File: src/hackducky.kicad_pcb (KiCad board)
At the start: 2 copper layers, 21 x 47 mm, 51 parts, among them J1 USB_A, J2 Conn_02x02_Top_Bottom, J3 Micro_SD_Card, P2 USB_C_Plug, SW3 BOOT_SEL, SW4 BOOT_SEL, U1 W25Q16JVSS, U2 AP2112K-3.3, U3 USBLC6-2P6, U4 RP2040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

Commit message: new sm fic
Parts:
- moved G*** 1.70 mm to (82.7, 95.0) (x2)
- moved G*** 0.26 mm to (82.1, 93.0)
- moved G*** 0.25 mm to (82.1, 93.0)
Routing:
- net +3V3: track 154.5 -> 138.2 mm, vias 23 -> 20
- net GPIO0: track 19.9 -> 14.4 mm, vias 3 -> 1
- net D-: track 47.8 -> 44.9 mm, vias 4 -> 2
- net D+: track 47.8 -> 44.9 mm, vias 4 -> 2
- net GND: track 189.5 -> 191.8 mm, vias 32 -> 29
- net GPIO11: track 6.53 -> 4.35 mm
- net SD_CLK: track 18.8 -> 19.6 mm
- net QSPI_SS: track 9.80 -> 10.5 mm, vias 3 -> 2
- net +5V: track 74.1 -> 74.4 mm, vias 6 -> 8
- added copper zone on B.Cu, net +3V3

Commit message: new
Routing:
- net GND: vias 29 -> 31
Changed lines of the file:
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@@
+	)
+	(via
+		(at 90 80.75)
+		(size 0.5)
+		(drill 0.3)
+		(layers "F.Cu" "B.Cu")
+		(net 1)
 	)
 	(via
@@
 		(drill 0.3)
 		(layers "F.Cu" "B.Cu")
+		(net 1)
+	)
+	(via
+		(at 90 80.75)
+		(size 0.5)
+		(drill 0.3)
+		(layers "F.Cu" "B.Cu")

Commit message: new
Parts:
- removed the G*** at (82.1, 93.0) (x2)
- removed the G*** at (82.7, 95.0) (x2)
- moved C12 1.81 mm to (82.8, 87.1), turned to 0 degrees
- moved R9 1.42 mm to (88.5, 85.8)
- moved C13 1.21 mm to (86.5, 85.5), turned to 180 degrees
- moved Y1 1.10 mm to (83.4, 84.9)
- moved D4 0.43 mm to (82.0, 81.8)
- moved D1 0.40 mm to (99.0, 80.5)
- moved R22 0.11 mm to (92.5, 74.6)
- moved R7 0.11 mm to (91.4, 74.6)
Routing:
- net +3V3: track 138.2 -> 128.6 mm, vias 20 -> 18
- net +1V1: track 27.8 -> 20.8 mm
- net Net-(C12-Pad1): track 7.71 -> 1.36 mm
- net GND: track 191.8 -> 186.2 mm, vias 31 -> 20
- net SD_CLK: track 19.6 -> 21.1 mm
- net XOUT: track 3.36 -> 1.89 mm
- net SD_MOSI: track 21.0 -> 22.2 mm
- net GP25: track 6.62 -> 5.98 mm

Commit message: fixed silkscren
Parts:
- added G*** (x2): LOGO, LOGO, F.Cu at (83.3, 92.8)
- added G*** (x2): LOGO, LOGO, B.Cu at (83.5, 95.9)

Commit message: new
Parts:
- moved C8 7.19 mm to (91.0, 79.3)
- moved C16 1.26 mm to (84.4, 68.0)
- moved G*** 0.29 mm to (82.6, 65.5)
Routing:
- net Net-(C12-Pad1): track 1.36 -> 8.22 mm
- net +1V1: track 20.8 -> 17.7 mm, vias 2 -> 3
- net +3V3: track 128.6 -> 125.5 mm
- net GND: track 186.2 -> 187.9 mm
- net QSPI_SS: track 10.5 -> 9.81 mm

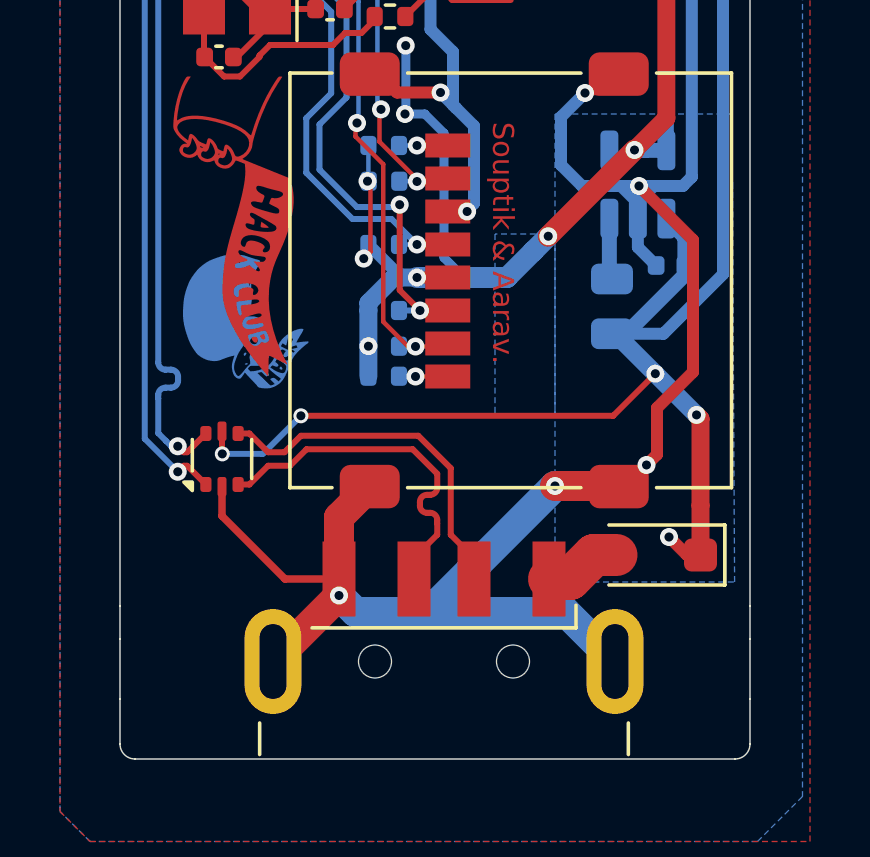
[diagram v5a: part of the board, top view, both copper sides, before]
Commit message: with bom corrected
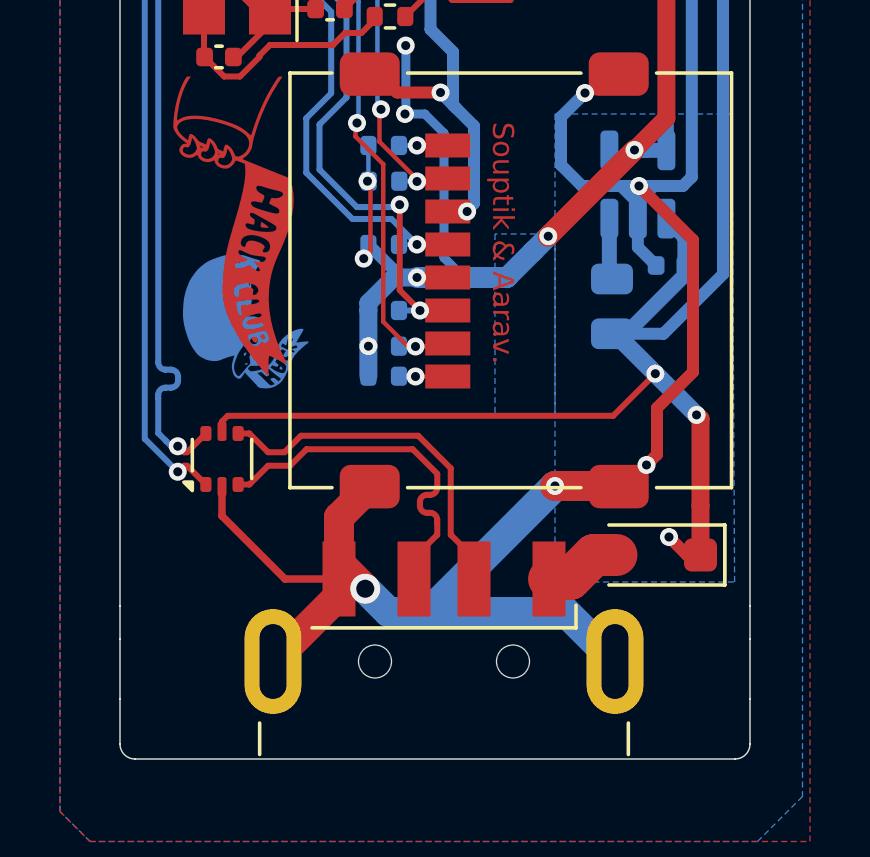
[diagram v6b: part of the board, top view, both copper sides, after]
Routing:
- net GND: track 187.9 -> 189.9 mm
- net +5V: track 74.4 -> 73.5 mm, vias 8 -> 6
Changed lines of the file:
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@@
 			(layer "F.Fab")
 		)
+		(fp_text user "${REFERENCE}"
+			(at 0 0 90)
+			(unlocked yes)
+			(layer "F.Fab")
+			(effects
+				(font
+					(size 1 1)
+					(thickness 0.15)
+				)
+			)
+		)
 		(pad "1" smd rect
 			(at -3.205 -2.1 90)
@@
 		)
 		(embedded_fonts no)
-		(model "${KICAD9_3DMODEL_DIR}/Connector_Card.3dshapes/microSD_HC_Hirose_DM3AT-SF-PEJM5.wrl"
+		(model "${KICAD9_3DMODEL_DIR}/Connector_Card.3dshapes/microSD_HC_Molex_47219-2001.wrl"
 			(offset
 				(xyz 0 0 0)
@@
 	)
 	(segment
+		(start 96.8 91.4)
+		(end 98.6 93.2)
+		(width 0.4)
+		(layer "F.Cu")
+		(net 1)
+	)
+	(segment
 		(start 96.105 101.4)
 		(end 96.125 101.42)
@@
 	)
 	(segment
-		(start 97.4 98.8)
-		(end 97.4 100.35)
-		(width 0.4)
-		(layer "F.Cu")
-		(net 1)
-	)
-	(segment
 		(start 83.52 79.25)
 		(end 83.35 79.25)
@@
 	)
 	(segment
+		(start 98.6 97.6)
+		(end 97.4 98.8)
+		(width 0.4)
+		(layer "F.Cu")
+		(net 1)
+	)
+	(segment
 		(start 94.11 73.69)
 		(end 94.2 73.69)
@@
 	)
 	(segment
-		(start 96.8 91.4)
-		(end 98.6 93.2)
-		(width 0.4)
-		(layer "F.Cu")
-		(net 1)
-	)
-	(segment
 		(start 94 101.4)
 		(end 96.105 101.4)
@@
 	)
 	(segment
+		(start 97.4 98.8)
+		(end 97.4 100.35)
+		(width 0.4)
+		(layer "F.Cu")
+		(net 1)
+	)
+	(segment
 		(start 90.16 72.5)
 		(end 90.16 70.325)
@@
 	)
 	(segment
-		(start 98.6 93.2)
-		(end 98.6 97.6)
-		(width 0.4)
-		(layer "F.Cu")
-		(net 1)
-	)
-	(segment
 		(start 88.98 68.3)
 		(end 88.98 67.75)
@@
 	)
 	(segment
+		(start 86.8 105.05)
+		(end 86.8 104.5)
+		(width 1)
+		(layer "F.Cu")
+		(net 1)
+	)
+	(segment
 		(start 84.5 86)
 		(end 84.5 85.75)
@@
 	)
 	(segment
+		(start 86.8 103.95)
+		(end 86.8 102.445)
+		(width 1)
+		(layer "F.Cu")
+		(net 1)
+	)
+	(segment
 		(start 85.286188 67.75)
 		(end 86.02 67.75)
@@
 	)
 	(segment
+		(start 87.675 104.825)
+		(end 86.8 103.95)
+		(width 1)
+		(layer "F.Cu")
+		(net 1)
+	)
+	(segment
 		(start 93.475 70.3)
 		(end 95.6 70.3)
@@
 	)
 	(segment
-		(start 86.8 104.5)
-		(end 86.8 105.05)
-		(width 1)
+		(start 98.6 93.2)
+		(end 98.6 97.6)
+		(width 0.4)
 		(layer "F.Cu")
 		(net 1)
@@
 	)
 	(segment
-		(start 83.28 87.1)
-		(end 83.4 87.1)
-		(width 0.2)
-		(layer "F.Cu")
-		(net 1)
-	)
-	(segment
-		(start 86.8 105.05)
-		(end 84.6 107.25)
+		(start 84.6 107.25)
+		(end 86.8 105.05)
 		(width 1)
 		(layer "F.Cu")
@@
 	)
 	(segment
-		(start 98.6 97.6)
-		(end 97.4 98.8)
-		(width 0.4)
+		(start 83.28 87.1)
+		(end 83.4 87.1)
+		(width 0.2)
 		(layer "F.Cu")
 		(net 1)
@@
 	)
 	(via
+		(at 87.675 104.825)
+		(size 1)
+		(drill 0.6)
+		(layers "F.Cu" "B.Cu")
+		(net 1)
+	)
+	(via
 		(at 83.1 79)
 		(size 0.6)
@@
 	)
 	(via
-		(at 86.8 105.05)
-		(size 0.6)
-		(drill 0.3)
-		(layers "F.Cu" "B.Cu")
-		(net 1)
-	)
-	(via
 		(at 96.8 91.4)
 		(size 0.6)
@@
 	)
 	(segment
+		(start 87.675 104.825)
+		(end 88.45 105.6)
+		(width 1)
+		(layer "B.Cu")
+		(net 1)
+	)
+	(segment
 		(start 87.229 65.121)
 		(end 87 65.35)
@@
 	)
 	(segment
-		(start 87.35 105.6)
-		(end 89.8 105.6)
-		(width 1)
-		(layer "B.Cu")
-		(net 1)
-	)
-	(segment
 		(start 94.2 90.7)
 		(end 94.9 91.4)
@@
 	)
 	(segment
+		(start 96.8 91.4)
+		(end 97.4 91.4)
+		(width 0.4)
+		(layer "B.Cu")
+		(net 1)
+	)
+	(segment
 		(start 98.55 79.5)
 		(end 98.56 79.51)
@@
 	)
 	(segment
-		(start 96.8 91.4)
-		(end 97.4 91.4)
-		(width 0.4)
-		(layer "B.Cu")
-		(net 1)
-	)
-	(segment
 		(start 98.56 91.1)
 		(end 98.26 91.4)
@@
 	)
 	(segment
+		(start 96.7625 91.4375)
+		(end 96.7625 92.4875)
+		(width 0.4)
+		(layer "B.Cu")
+		(net 1)
+	)
+	(segment
 		(start 90.16 70.99)
 		(end 90.4 70.75)
@@
 	)
 	(segment
-		(start 96.7625 92.4875)
-		(end 96.7625 91.4375)
-		(width 0.4)
-		(layer "B.Cu")
-		(net 1)
-	)
-	(segment
 		(start 92.729 64.64)
 		(end 92.729 65.079)
@@
 	)
 	(segment
+		(start 88.45 105.6)
+		(end 89.8 105.6)
+		(width 1)
+		(layer "B.Cu")
+		(net 1)
+	)
+	(segment
+		(start 96.8 91.4)
+		(end 96.7625 91.4375)
+		(width 0.4)
+		(layer "B.Cu")
+		(net 1)
+	)
+	(segment
 		(start 90.6 88.7)
 		(end 90.6 86.93)
@@
 	)
 	(segment
-		(start 96.7625 91.4375)
+		(start 96.2 91.4)
 		(end 96.8 91.4)
 		(width 0.4)
@@
 	)
 	(segment
-		(start 86.8 105.05)
-		(end 87.35 105.6)
-		(width 1)
-		(layer "B.Cu")
-		(net 1)
-	)
-	(segment
 		(start 89.85 86.18)
 		(end 89.85 83.55)
@@
 	)
 	(segment
-		(start 96.2 91.4)
-		(end 96.8 91.4)
-		(width 0.4)
-		(layer "B.Cu")
-		(net 1)
-	)
-	(segment
 		(start 93.12 75.48)
 		(end 93.5 75.48)
@@
 	)
 	(segment
-		(start 82.9 99.575)
-		(end 82.9 100.32)
-		(width 0.2)
-		(layer "F.Cu")
-		(net 6)
-	)
-	(segment
 		(start 95.94 99.06)
 		(end 97.34375 97.65625)
@@
 	)
 	(segment
-		(start 94.07 68.63)
-		(end 94.08 68.64)
-		(width 0.3)
+		(start 82.9 99.250001)
+		(end 83.090001 99.06)
+		(width 0.2)
 		(layer "F.Cu")
 		(net 6)
 	)
 	(segment
-		(start 82.9 100.32)
-		(end 82.91 100.33)
+		(start 83.090001 99.06)
+		(end 95.94 99.06)
 		(width 0.2)
 		(layer "F.Cu")
@@
 	)
 	(segment
-		(start 85.53 99.06)
-		(end 95.94 99.06)
-		(width 0.2)
+		(start 94.07 68.63)
+		(end 94.08 68.64)
+		(width 0.3)
 		(layer "F.Cu")
 		(net 6)
@@
 	)
 	(segment
+		(start 82.9 99.575)
+		(end 82.9 99.250001)
+		(width 0.2)
+		(layer "F.Cu")
+		(net 6)
+	)
+	(segment
 		(start 98.5 66.1)
 		(end 98.5 65.05)
@@
 	)
 	(via
-		(at 82.91 100.33)
-		(size 0.5)
-		(drill 0.3)
-		(layers "F.Cu" "B.Cu")
-		(net 6)
-	)
-	(via
-		(at 85.53 99.06)
-		(size 0.5)
-		(drill 0.3)
-		(layers "F.Cu" "B.Cu")
-		(net 6)
-	)
-	(via
 		(at 97.8 103.1)
 		(size 0.6)
@@
 	)
 	(segment
-		(start 84.26 100.33)
-		(end 82.91 100.33)
-		(width 0.2)
-		(layer "B.Cu")
-		(net 6)
-	)
-	(segment
 		(start 97.615 96.325)
 		(end 95.9 96.325)
@@
 		(layer "B.Cu")
 		(net 6)
-	)
-	(segment
-		(start 85.53 99.06)
-		(end 84.26 100.33)
-		(width 0.2)
-		(layer "B.Cu")
-		(net 6)
